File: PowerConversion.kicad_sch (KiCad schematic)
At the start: 25 parts, among them IC401 TPS563200DDCR, IC402 LM74700QDBVTQ1, Q401 60V 38A, U401 LDO 3.3V 1A

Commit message: Updated symbols, added jobset and output folders.
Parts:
- C401, C402, C404, C409, C411: Manufacturer (none) -> Samsung Electro-Mechanics; Manufacturer Part No (none) -> CL31A106KBHNNNE
- R401: Manufacturer (none) -> UNI-ROYAL(Uniroyal Elec); Manufacturer Part No (none) -> 0805W8F3300T5E
- R402: Manufacturer (none) -> YAGEO; Manufacturer Part No (none) -> RC1206FR-0756KL
- TP401, TP402, TP403, TP404: now left out of the parts list
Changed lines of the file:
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@@
 		(unit 1)
 		(exclude_from_sim no)
-		(in_bom yes)
+		(in_bom no)
 		(on_board yes)
 		(dnp no)
@@
 		(unit 1)
 		(exclude_from_sim no)
-		(in_bom yes)
+		(in_bom no)
 		(on_board yes)
 		(dnp no)
@@
 			)
 		)
+		(property "Manufacturer" "Samsung Electro-Mechanics"
+			(at 951.46 59.69 0)
+			(effects
+				(font
+					(size 1.27 1.27)
+				)
+				(justify left top)
+				(hide yes)
+			)
+		)
+		(property "Manufacturer Part No" "CL31A106KBHNNNE"
+			(at 1051.46 59.69 0)
+			(effects
+				(font
+					(size 1.27 1.27)
+				)
+				(justify left top)
+				(hide yes)
+			)
+		)
 		(pin "2"
 		)
@@
 			)
 		)
+		(property "Manufacturer" "Samsung Electro-Mechanics"
+			(at -583.16 132.08 0)
+			(effects
+				(font
+					(size 1.27 1.27)
+				)
+				(justify left top)
+				(hide yes)
+			)
+		)
+		(property "Manufacturer Part No" "CL31A106KBHNNNE"
+			(at -683.16 132.08 0)
+			(effects
+				(font
+					(size 1.27 1.27)
+				)
+				(justify left top)
+				(hide yes)
+			)
+		)
 		(pin "2"
 		)
@@
 	)
 	(symbol
-		(lib_name "CC0603KRX7R9BB104_1")
 		(lib_id "JLCPCB Basic:CC0603KRX7R9BB104")
 		(at 111.76 59.69 90)
@@
 			)
 		)
+		(property "Manufacturer" "YAGEO"
+			(at 834.62 44.45 0)
+			(effects
+				(font
+					(size 1.27 1.27)
+				)
+				(justify left top)
+				(hide yes)
+			)
+		)
+		(property "Manufacturer Part No" "RC1206FR-0756KL"
+			(at 934.62 44.45 0)
+			(effects
+				(font
+					(size 1.27 1.27)
+				)
+				(justify left top)
+				(hide yes)
+			)
+		)
 		(pin "2"
 		)
@@
 		(unit 1)
 		(exclude_from_sim no)
-		(in_bom yes)
+		(in_bom no)
 		(on_board yes)
 		(dnp no)
@@
 			)
 		)
+		(property "Manufacturer" "Samsung Electro-Mechanics"
+			(at -655.55 60.96 0)
+			(effects
+				(font
+					(size 1.27 1.27)
+				)
+				(justify left top)
+				(hide yes)
+			)
+		)
+		(property "Manufacturer Part No" "CL31A106KBHNNNE"
+			(at -755.55 60.96 0)
+			(effects
+				(font
+					(size 1.27 1.27)
+				)
+				(justify left top)
+				(hide yes)
+			)
+		)
 		(pin "2"
 		)
@@
 			)
 		)
+		(property "Manufacturer" "UNI-ROYAL(Uniroyal Elec)"
+			(at 113.03 805.41 0)
+			(effects
+				(font
+					(size 1.27 1.27)
+				)
+				(justify left top)
+				(hide yes)
+			)
+		)
+		(property "Manufacturer Part No" "0805W8F3300T5E"
+			(at 113.03 905.41 0)
+			(effects
+				(font
+					(size 1.27 1.27)
+				)
+				(justify left top)
+				(hide yes)
+			)
+		)
 		(pin "1"
 		)
@@
 	)
 	(symbol
-		(lib_name "CC0603KRX7R9BB104_2")
 		(lib_id "JLCPCB Basic:CC0603KRX7R9BB104")
 		(at 181.61 120.65 270)
@@
 		(unit 1)
 		(exclude_from_sim no)
-		(in_bom yes)
+		(in_bom no)
 		(on_board yes)
 		(dnp no)
@@
 			)
 		)
+		(property "Manufacturer" "Samsung Electro-Mechanics"
+			(at -505.69 129.54 0)
+			(effects
+				(font
+					(size 1.27 1.27)
+				)
+				(justify left top)
+				(hide yes)
+			)
+		)
+		(property "Manufacturer Part No" "CL31A106KBHNNNE"
+			(at -605.69 129.54 0)
+			(effects
+				(font
+					(size 1.27 1.27)
+				)
+				(justify left top)
+				(hide yes)
+			)
+		)
 		(pin "2"
 		)
@@
 	)
 	(symbol
-		(lib_name "0805W8F1002T5E_1")
 		(lib_id "JLCPCB Basic:0805W8F1002T5E")
 		(at 165.1 139.7 0)
@@
 				(hide yes)
 			)
+		)
+		(property "Manufacturer" "Samsung Electro-Mechanics"
+			(at -647.93 60.96 0)
+			(effects
+				(font
+					(size 1.27 1.27)
+				)
+				(justify left top)
+				(hide yes)
+			)
+		)
+		(property "Manufacturer Part No" "CL31A106KBHNNNE"
+			(at -747.93 60.96 0)
+			(effects
+				(font
+					(size 1.27 1.27)
+				)
+				(justify left top)
+				(hide yes)
+			)

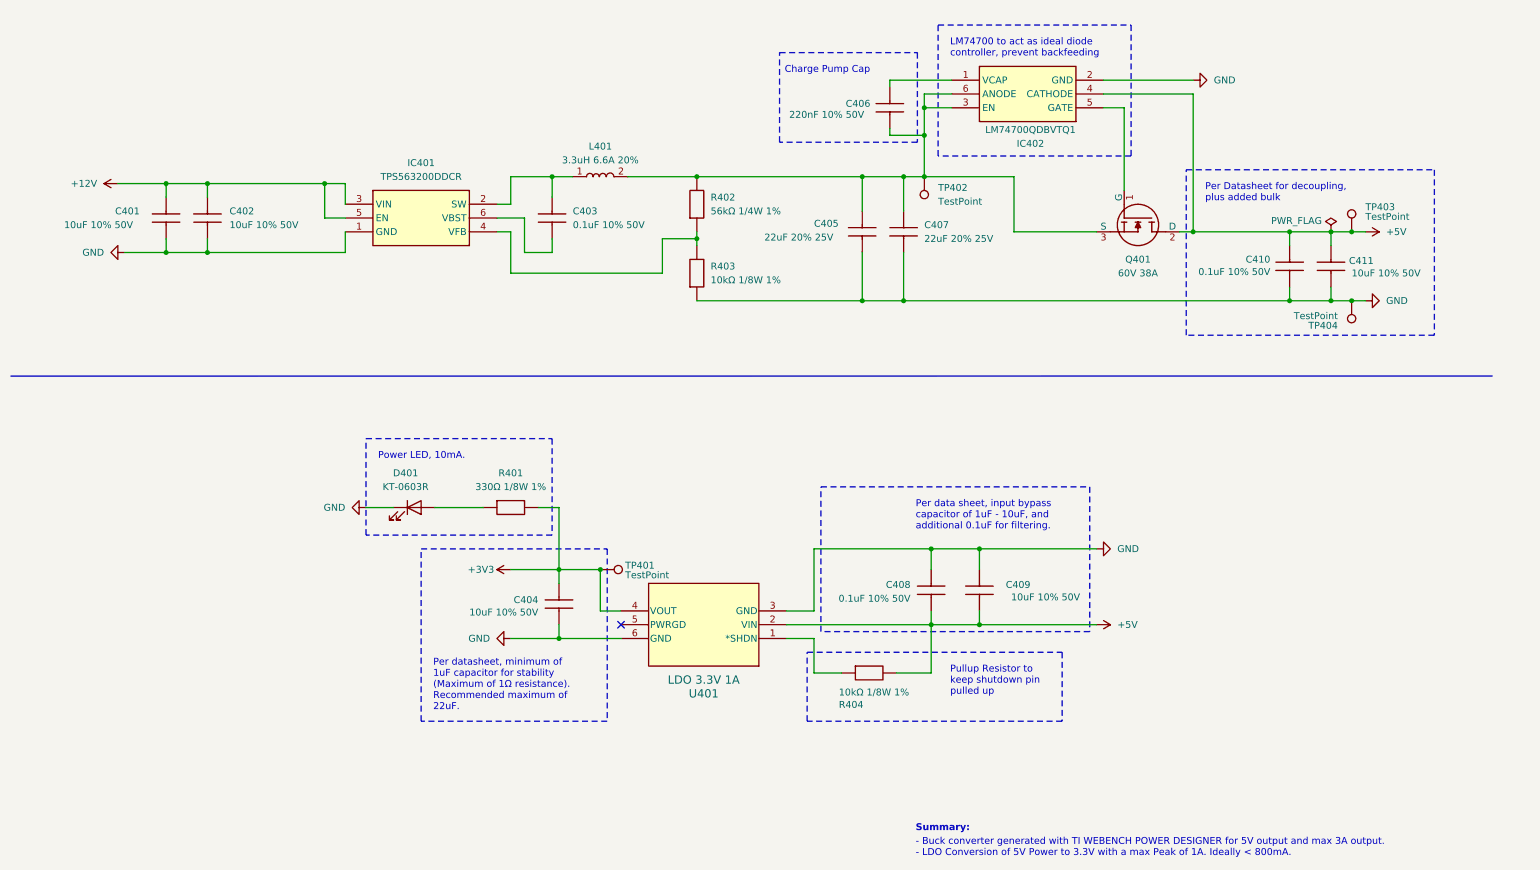
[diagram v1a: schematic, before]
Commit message: Updated inductor component and 10uF capacitor components to bring down cost.
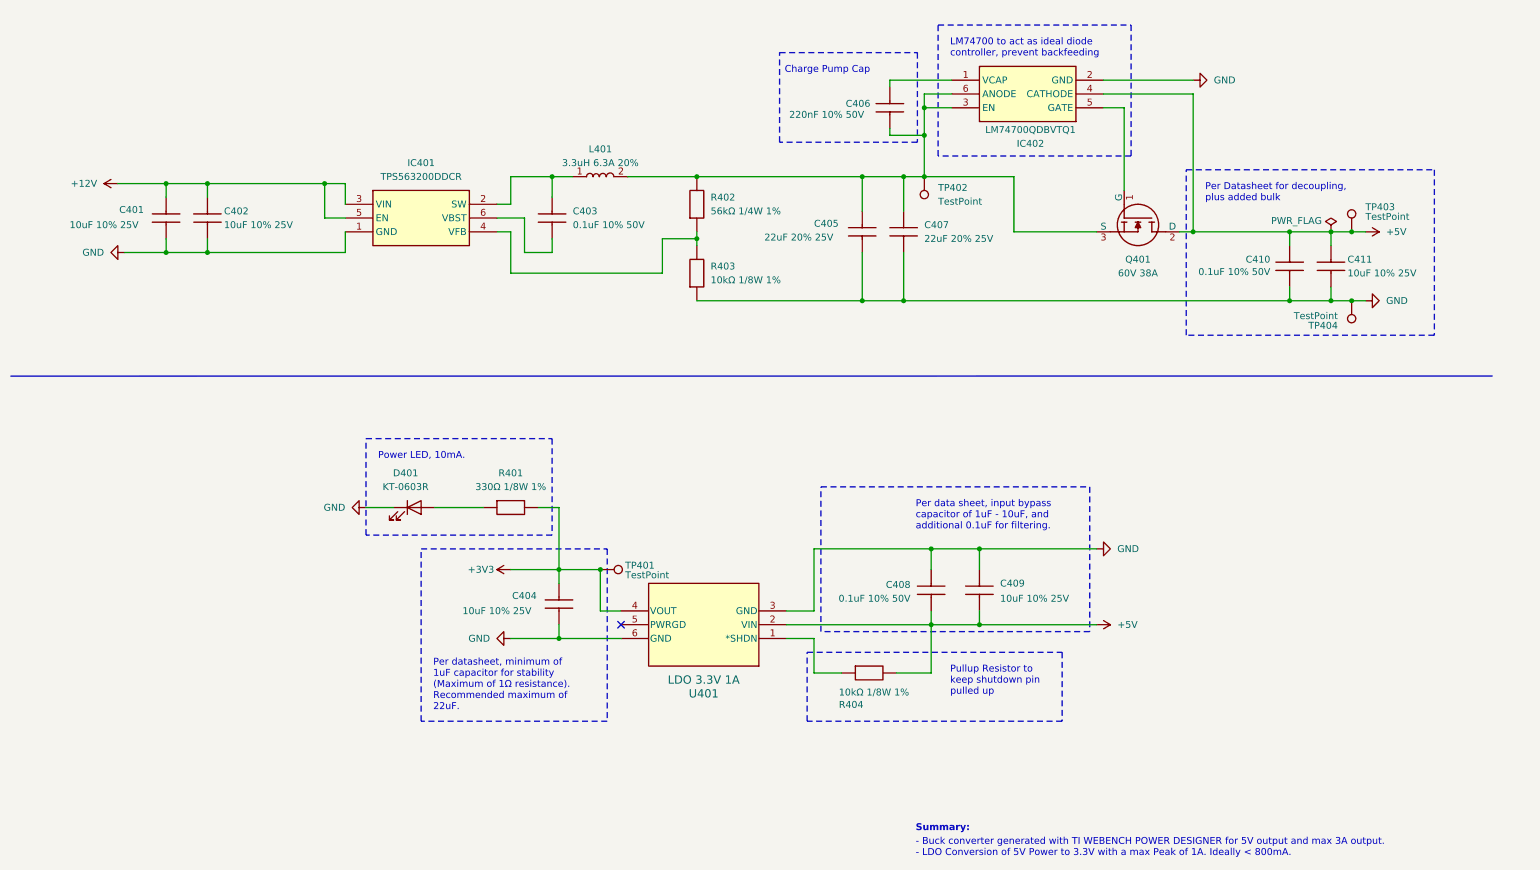
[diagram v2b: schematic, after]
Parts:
- removed C401, C402, C404, C409, C411: 10uF 10% 50V, JLCPCB Basic:CAPC3216X180N, symbol JLCPCB Basic:CL31A106KBHNNNE
- removed L401: 3.3uH 6.6A 20%, COILCRAFT Inductors:XAL40XX, symbol COILCRAFT Inductors:XAL4030-332MEC
- added C401, C402, C404, C409, C411: 10uF 10% 25V, JLCPCB Basic:CAPC3216X180N, symbol SAMSUNGELECTROMECHANICS Resistors:CL31A106KAHNNNE
- added L401: 3.3uH 6.3A 20%, KOHERELEC Inductors:SMD57x52mm, symbol KOHERELEC Inductors:MDA5030-3R3M
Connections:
- net +12V: now also C401.2, C402.2
- net +3V3: now also C404.2
- net +5V: now also C409.1, C411.2
- net GND: now also C401.1, C402.1, C404.1, C409.2, C411.1
- net at C405.2, C406.2, C407.2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: now also L401.2
- net at C403.2, IC401.2 (SW): now also L401.1

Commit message: Updated schematic to use a different TPS54308 buck instead.
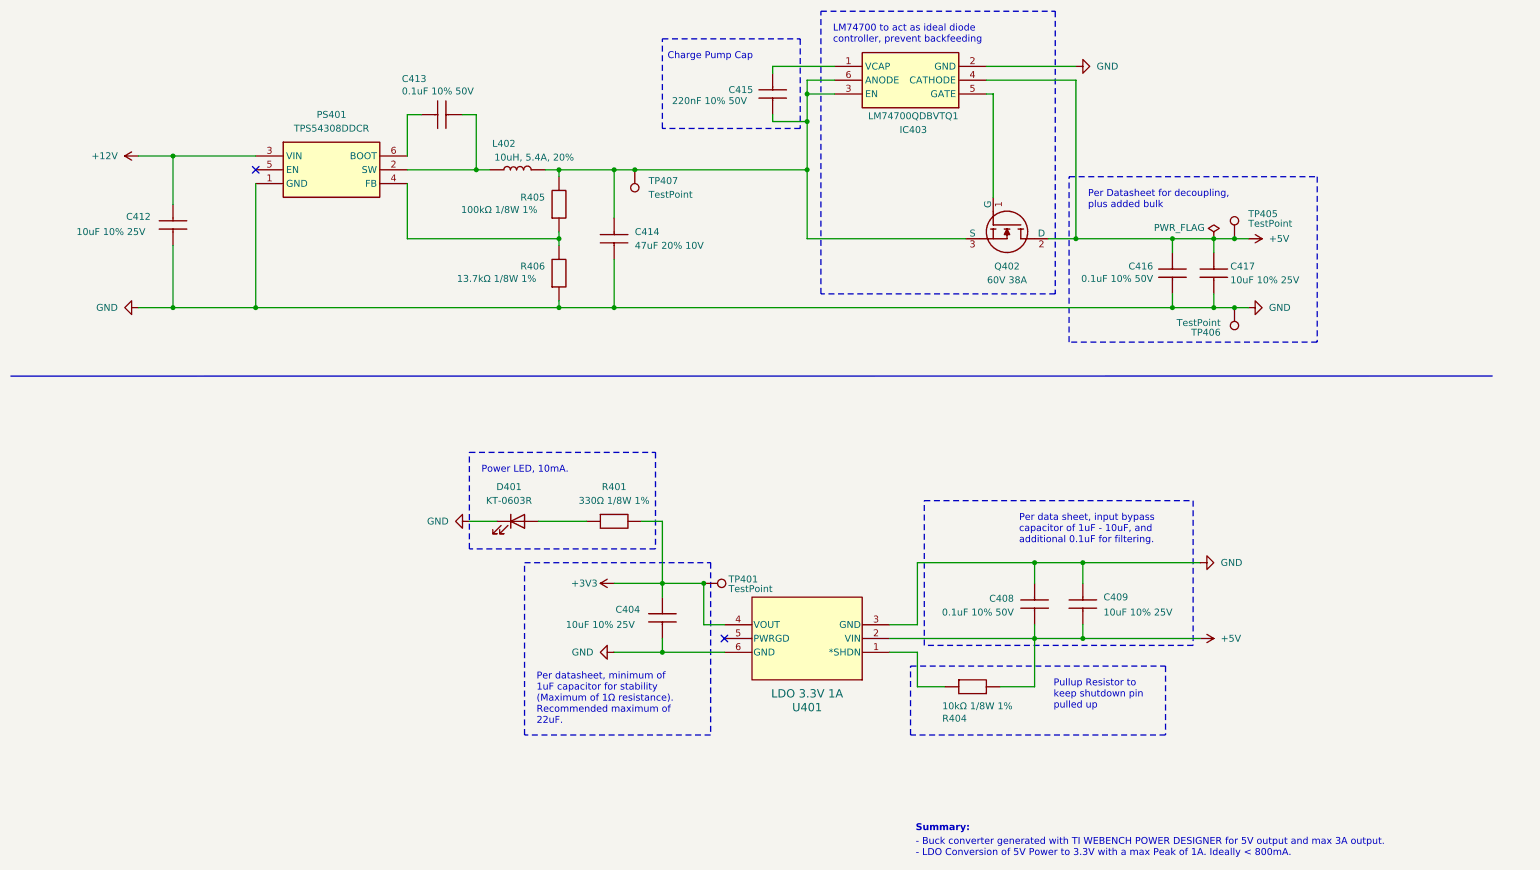
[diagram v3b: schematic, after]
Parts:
- removed C401, C402, C411: 10uF 10% 25V, JLCPCB Basic:CAPC3216X180N, symbol SAMSUNGELECTROMECHANICS Resistors:CL31A106KAHNNNE
- removed C403, C410: 0.1uF 10% 50V, JLCPCB Basic:CAPC1608X90N, symbol JLCPCB Basic:CC0603KRX7R9BB104
- removed C405, C407: 22uF 20% 25V, JLCPCB Basic:CAPC2012X75N, symbol JLCPCB Basic:CL21A226MAQNNNE
- removed C406: 220nF 10% 50V, JLCPCB Basic:CAPC2012X135N, symbol JLCPCB Basic:CL21B224KBFNNNE
- removed IC401: TPS563200DDCR, TEXAS INSTRUMENTS ICs:SOT95P280X110-6N, symbol TEXAS INSTRUMENTS ICs:TPS563200DDCR
- removed IC402: LM74700QDBVTQ1, TEXAS INSTRUMENTS ICs:SOT95P280X145-6N, symbol TEXAS INSTRUMENTS ICs:LM74700QDBVTQ1
- removed L401: 3.3uH 6.3A 20%, KOHERELEC Inductors:SMD57x52mm, symbol KOHERELEC Inductors:MDA5030-3R3M
- removed Q401: 60V 38A, ONSEMI Transistors:DPAK__SINGLE-GAUGE__TO-252_369C__ISSUE_F, symbol ONSEMI Transistors:NVD5C684NLT4G
- removed R402: 56kΩ 1/4W 1%, YAGEO Resistors:RESC3116X65N, symbol YAGEO Resistors:RC1206FR-0756KL
- removed R403: 10kΩ 1/8W 1%, JLCPCB Basic:RESC2013X65N, symbol JLCPCB Basic:0805W8F1002T5E
- removed TP402, TP403, TP404: TestPoint, TestPoint:TestPoint_Pad_2.0x2.0mm, symbol Connector:TestPoint
- added C412, C417: 10uF 10% 25V, JLCPCB Basic:CAPC3216X180N, symbol SAMSUNGELECTROMECHANICS Resistors:CL31A106KAHNNNE
- added C413, C416: 0.1uF 10% 50V, JLCPCB Basic:CAPC1608X90N, symbol JLCPCB Basic:CC0603KRX7R9BB104
- added C414: 47uF 20% 10V, JLCPCB Basic:CAPC3216X190N, symbol JLCPCB Basic:CL31A476MPHNNNE
- added C415: 220nF 10% 50V, JLCPCB Basic:CAPC2012X135N, symbol JLCPCB Basic:CL21B224KBFNNNE
- added IC403: LM74700QDBVTQ1, TEXAS INSTRUMENTS ICs:SOT95P280X145-6N, symbol TEXAS INSTRUMENTS ICs:LM74700QDBVTQ1
- added L402: 10uH, 5.4A, 20%, Inductor_SMD:L_SXN_SMDRI127, symbol SXN Inductors:SMDRI127-100MT
- added PS401: TPS54308DDCR, TEXAS INSTRUMENTS ICs:SOT95P280X110-6N, symbol TEXAS INSTRUMENTS ICs:TPS54308DDCR
- added Q402: 60V 38A, ONSEMI Transistors:DPAK__SINGLE-GAUGE__TO-252_369C__ISSUE_F, symbol ONSEMI Transistors:NVD5C684NLT4G
- added R405: 100kΩ 1/8W 1%, JLCPCB Basic:RESC2013X65N, symbol JLCPCB Basic:0805W8F1003T5E
- added R406: 13.7kΩ 1/8W 1%, YAGEO Resistors:RESC2012X60N, symbol YAGEO Resistors:AC0805FR-0713K7L
- added TP405, TP406, TP407: TestPoint, TestPoint:TestPoint_Pad_2.0x2.0mm, symbol Connector:TestPoint
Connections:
- net +12V: now also C412.2, PS401.3 (VIN)
- net +5V: now also C416.2, C417.2, IC403.4 (CATHODE), Q402.2 (D), Q402.4 (D), TP405.1
- net GND: now also C412.1, C414.1, C416.1, C417.1, IC403.2 (GND), PS401.1 (GND), R406.1, TP406.1
- new net: C414.2, C415.2, IC403.3 (EN), IC403.6 (ANODE), L402.2, Q402.3 (S), R405.2, TP407.1
- new net: C415.1, IC403.1 (VCAP)
- new net: PS401.4 (FB), R405.1, R406.2
- new net: C413.1, L402.1, PS401.2 (SW)
- new net: C413.2, PS401.6 (BOOT)
- new net: IC403.5 (GATE), Q402.1 (G)
- no-connect marks 1 -> 2
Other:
- moved on the sheet: C404, C408, C409, D401, R401, R404, TP401, U401

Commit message: Swapped MCP1826 with a TLV767, and updated the layout and silkscreen to match it.
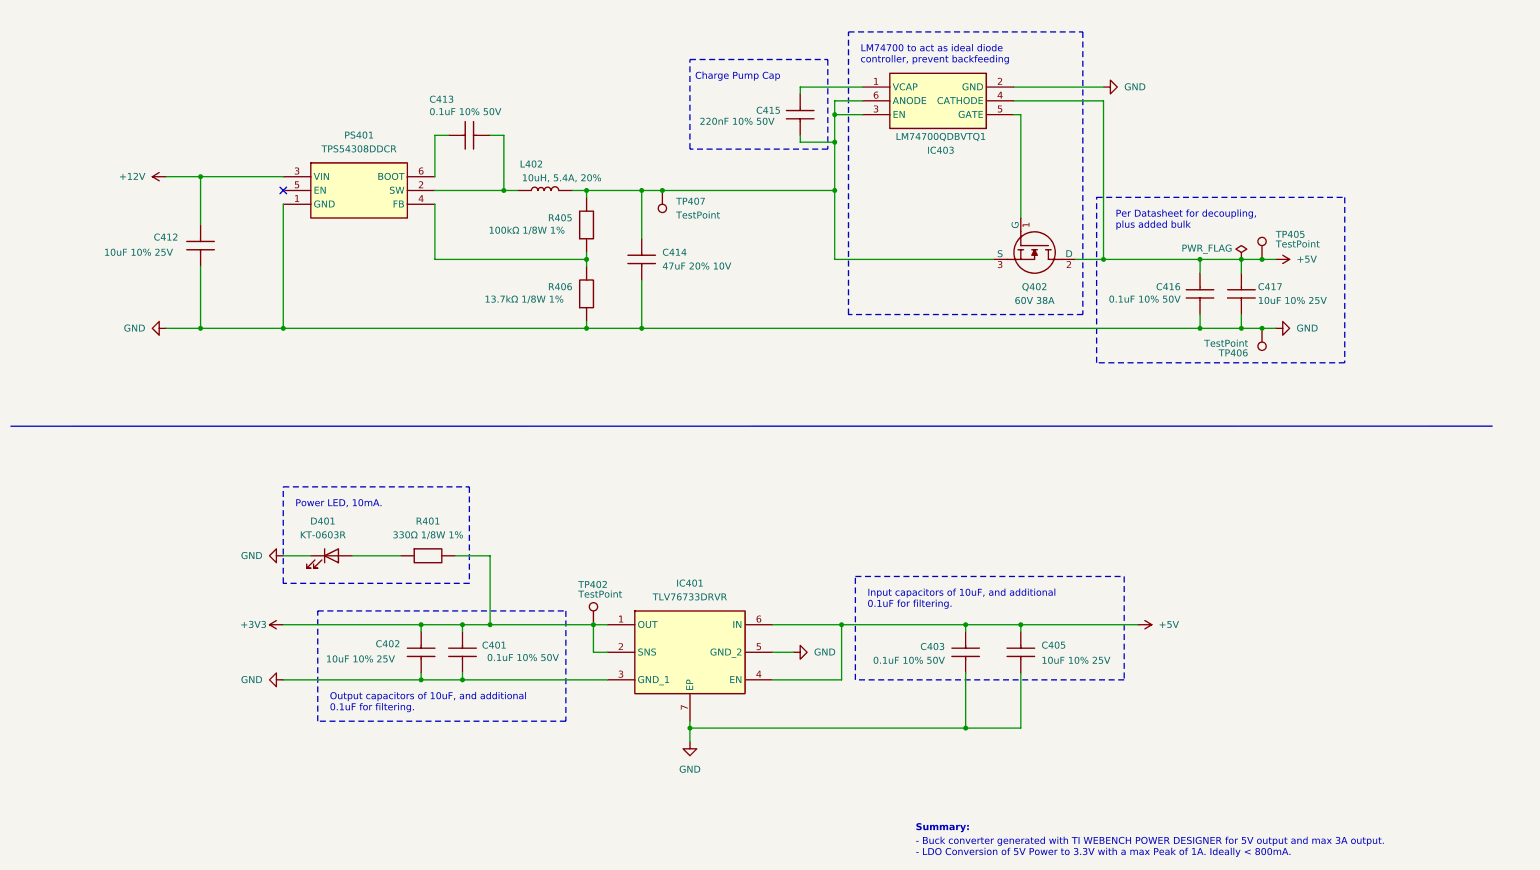
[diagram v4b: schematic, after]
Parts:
- removed C404, C409: 10uF 10% 25V, JLCPCB Basic:CAPC3216X180N, symbol SAMSUNGELECTROMECHANICS Resistors:CL31A106KAHNNNE
- removed C408: 0.1uF 10% 50V, JLCPCB Basic:CAPC1608X90N, symbol JLCPCB Basic:CC0603KRX7R9BB104
- removed R404: 10kΩ 1/8W 1%, JLCPCB Basic:RESC2013X65N, symbol JLCPCB Basic:0805W8F1002T5E
- removed TP401: TestPoint, TestPoint:TestPoint_Pad_2.0x2.0mm, symbol Connector:TestPoint
- removed U401: LDO 3.3V 1A, MICROCHIPTECH Low Dropout Regulators:DDPAK5_MC_MCH, symbol MICROCHIPTECH Low Dropout Regulators:MCP1826-3302E_ET
- added C401, C403: 0.1uF 10% 50V, JLCPCB Basic:CAPC1608X90N, symbol JLCPCB Basic:CC0603KRX7R9BB104
- added C402, C405: 10uF 10% 25V, JLCPCB Basic:CAPC3216X180N, symbol SAMSUNGELECTROMECHANICS Resistors:CL31A106KAHNNNE
- added IC401: TLV76733DRVR, TEXAS INSTRUMENTS ICs:SON65P200X200X80-7N, symbol TEXAS INSTRUMENTS ICs:TLV76733DRVR
- added TP402: TestPoint, TestPoint:TestPoint_Pad_2.0x2.0mm, symbol Connector:TestPoint
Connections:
- net +3V3: now also C401.1, C402.2, IC401.1 (OUT), IC401.2 (SNS), TP402.1
- net +5V: now also C403.1, C405.2, IC401.4 (EN), IC401.6 (IN)
- net GND: now also C401.2, C402.1, C403.2, C405.1, IC401.3 (GND_1), IC401.5 (GND_2), IC401.7 (EP)
- no-connect marks 2 -> 1
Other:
- moved on the sheet: C412, C413, C414, C415, C416, C417, D401, IC403, L402, PS401, Q402, R401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

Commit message: Silkscreen Updates and BOM added
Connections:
- net GND: now also D401.2 (K); no longer D401.1 (K)
- net at R401.1: now also D401.1 (A); no longer D401.2 (A)
